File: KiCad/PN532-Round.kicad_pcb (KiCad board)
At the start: 2 copper layers, 46 x 46 mm, 52 parts, among them J1 Bell, J2 Bell, J3 TSM-104-02-L-SV, SW1 ESE13V01D, U1 PN532, U2 QR, Y1 27.12MHz

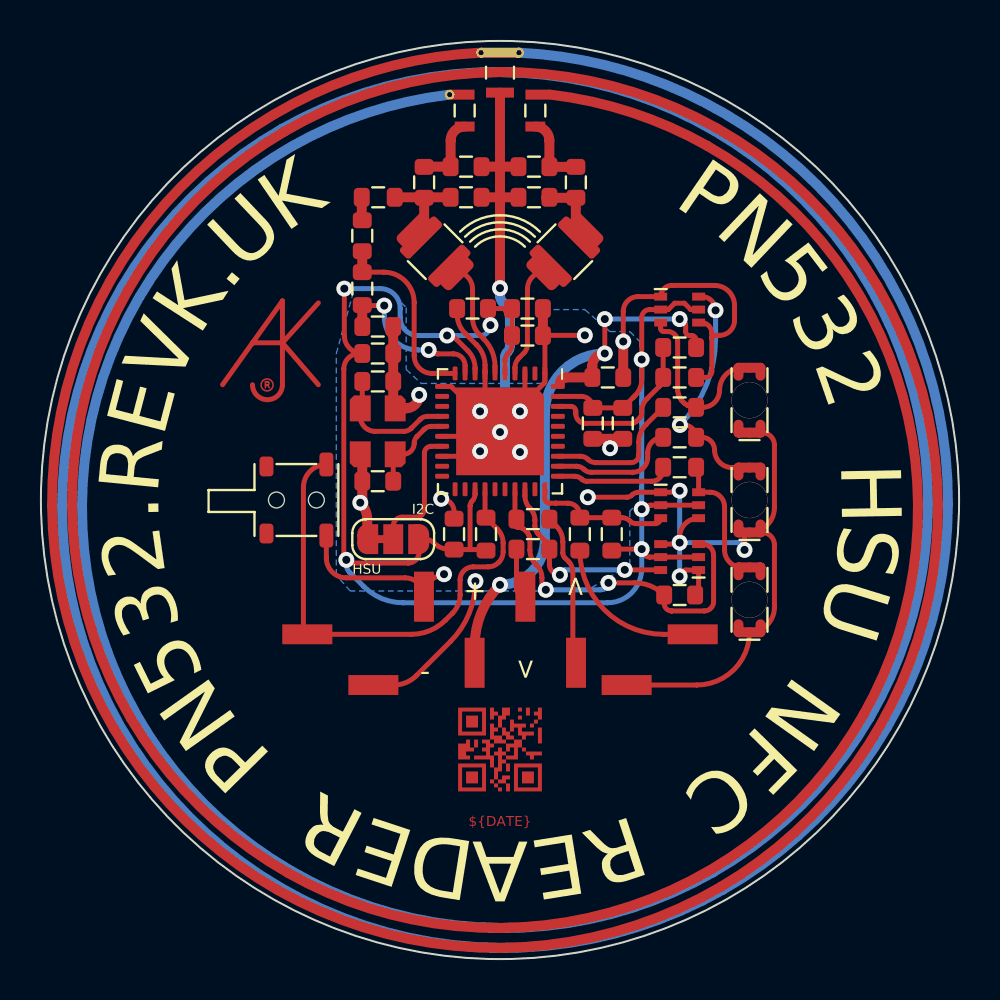
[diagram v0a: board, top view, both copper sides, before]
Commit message: Made bell part of connector, optional 4 or 5 way, and removed connector for tamper as not protected and good tamper switch now.
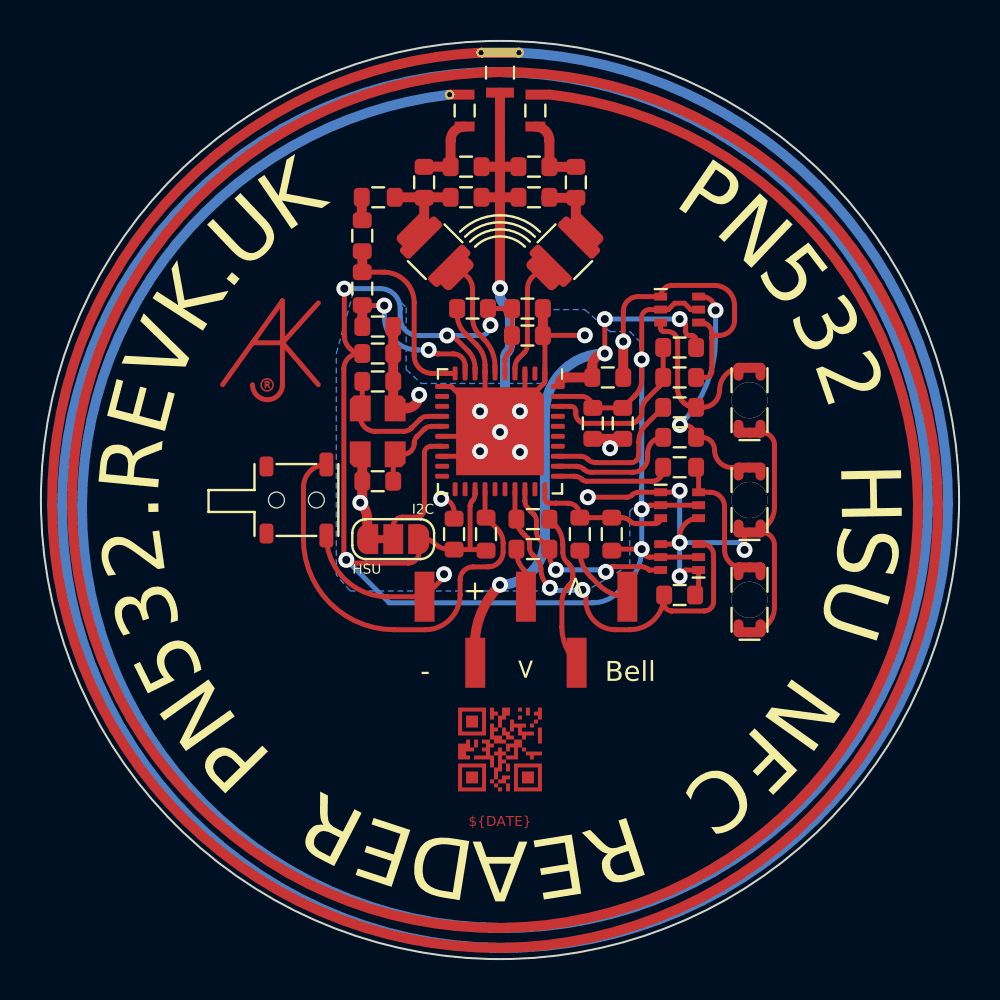
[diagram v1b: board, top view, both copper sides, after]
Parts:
- removed J1: Bell, RevK:PinHeader_1x02_P2.54mm_Vertical_SMD_Pin1Right
- removed J2: Bell, RevK:PinHeader_1x02_P2.54mm_Vertical_SMD_Pin1Left
- J3: value TSM-104-02-L-SV -> Conn; footprint RevK:PinHeader_1x04_P2.54mm_Vertical_SMD_Pin1Right -> RevK:PinHeader_1x05_P2.54mm_Vertical_SMD_Pin1Right
- moved J3 1.30 mm to (101.3, 106.5)
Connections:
- R12 pad 2: Net-(J1-Pad2) -> Net-(J3-Pad5)
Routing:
- net GND: track 128.3 -> 112.6 mm, vias 19 -> 18
- net Net-(J1-Pad2): track 8.38 -> 0.00 mm
- net Net-(J3-Pad5): track 0.00 -> 3.60 mm
- net Net-(R11-Pad2): track 24.8 -> 22.5 mm
- net Net-(C19-Pad1): track 18.6 -> 20.0 mm
- net +3V3: track 89.4 -> 88.9 mm
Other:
- board text added: "Bell"

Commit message: Revised connector
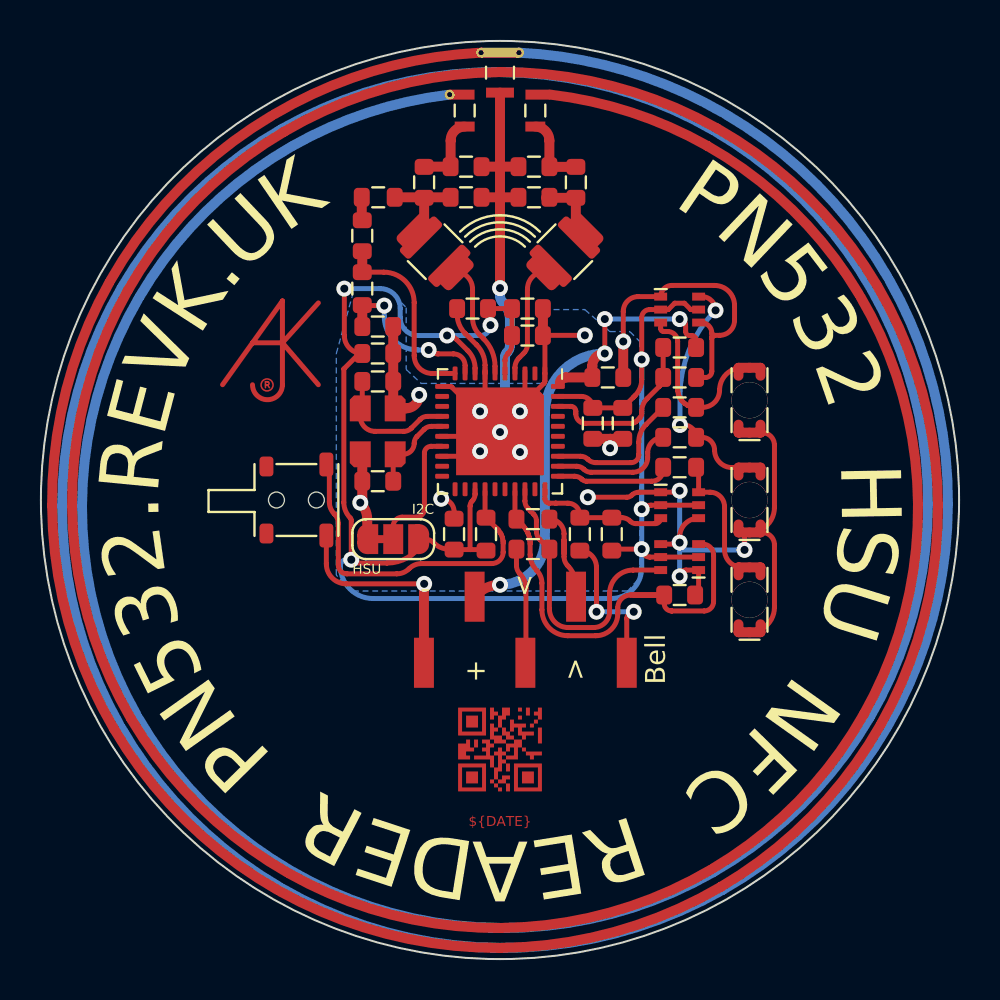
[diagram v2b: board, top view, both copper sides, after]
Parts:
- J3: footprint RevK:PinHeader_1x05_P2.54mm_Vertical_SMD_Pin1Right -> RevK:PinHeader_1x05_P2.54mm_Vertical_SMD_Pin1Left
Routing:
- net Net-(R11-Pad2): track 22.5 -> 17.5 mm
- net Net-(J3-Pad5): track 3.60 -> 8.11 mm, vias 0 -> 2
- net Net-(D6-Pad6): track 10.0 -> 14.4 mm, vias 2 -> 0
- net Net-(J3-Pad3): track 2.50 -> 5.81 mm
- net +5V: track 28.8 -> 26.1 mm
- net Net-(J3-Pad4): track 7.88 -> 5.12 mm
- net Net-(C19-Pad1): track 20.0 -> 22.7 mm, vias 2 -> 0
- net GND: track 112.6 -> 115.1 mm
- net +3V3: track 88.9 -> 89.5 mm
